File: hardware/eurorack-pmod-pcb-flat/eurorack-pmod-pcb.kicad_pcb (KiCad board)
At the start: 4 copper layers, 40 x 110 mm, 104 parts, among them J1 EURORACK_PWR, J10 PJ398SM, J2 PMOD, J3 PJ398SM, J4 PJ398SM, J5 PJ398SM, J6 PJ398SM, J7 PJ398SM, J8 PJ398SM, J9 PJ398SM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

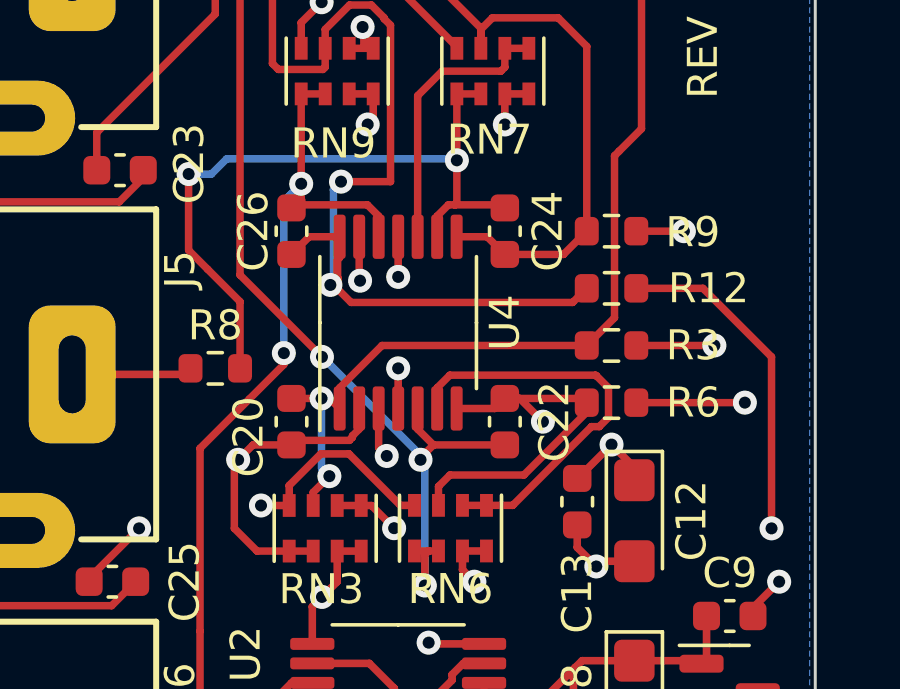
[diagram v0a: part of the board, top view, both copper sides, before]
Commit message: rev3: add notes, fix flipped op-amp
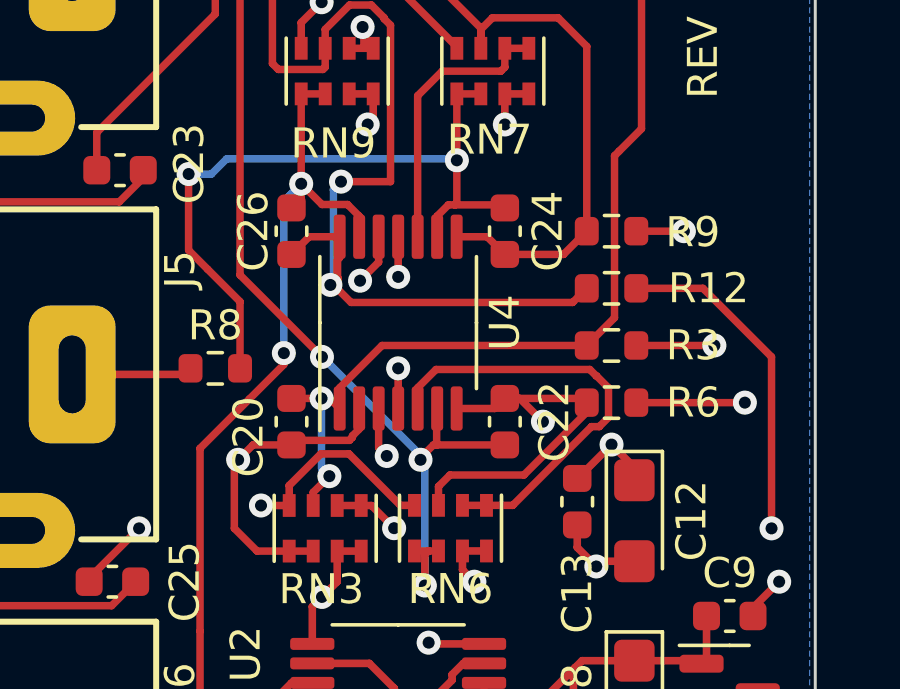
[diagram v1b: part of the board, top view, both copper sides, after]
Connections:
- U4 pad 12: Net-(C26-Pad1) -> Net-(RN9-Pad5)
- U4 pad 13: Net-(RN9-Pad5) -> Net-(C26-Pad1)
- U4 pad 5: Net-(C22-Pad1) -> Net-(RN6-Pad5)
- U4 pad 6: Net-(RN6-Pad5) -> Net-(C22-Pad1)
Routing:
- net Net-(RN6-Pad5): track 13.8 -> 14.6 mm
- net Net-(C26-Pad1): track 30.6 -> 29.9 mm
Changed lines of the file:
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@@
       (net 7 "+12V") (pinfunction "V+") (pintype "power_in"))
     (pad "5" smd roundrect (at -2.8625 0.65 90) (size 1.475 0.4) (layers "F.Cu" "F.Paste" "F.Mask") (roundrect_rratio 0.25)
-      (net 58 "Net-(C22-Pad1)") (pinfunction "+") (pintype "input"))
+      (net 49 "Net-(RN6-Pad5)") (pinfunction "+") (pintype "input"))
     (pad "6" smd roundrect (at -2.8625 1.3 90) (size 1.475 0.4) (layers "F.Cu" "F.Paste" "F.Mask") (roundrect_rratio 0.25)
-      (net 49 "Net-(RN6-Pad5)") (pinfunction "-") (pintype "input"))
+      (net 58 "Net-(C22-Pad1)") (pinfunction "-") (pintype "input"))
     (pad "7" smd roundrect (at -2.8625 1.95 90) (size 1.475 0.4) (layers "F.Cu" "F.Paste" "F.Mask") (roundrect_rratio 0.25)
       (net 59 "Net-(C22-Pad2)") (pintype "output"))
@@
       (net 8 "-12V") (pinfunction "V-") (pintype "power_in"))
     (pad "12" smd roundrect (at 2.8625 -0.65 90) (size 1.475 0.4) (layers "F.Cu" "F.Paste" "F.Mask") (roundrect_rratio 0.25)
-      (net 68 "Net-(C26-Pad1)") (pinfunction "+") (pintype "input"))
+      (net 82 "Net-(RN9-Pad5)") (pinfunction "+") (pintype "input"))
     (pad "13" smd roundrect (at 2.8625 -1.3 90) (size 1.475 0.4) (layers "F.Cu" "F.Paste" "F.Mask") (roundrect_rratio 0.25)
-      (net 82 "Net-(RN9-Pad5)") (pinfunction "-") (pintype "input"))
+      (net 68 "Net-(C26-Pad1)") (pinfunction "-") (pintype "input"))
     (pad "14" smd roundrect (at 2.8625 -1.95 90) (size 1.475 0.4) (layers "F.Cu" "F.Paste" "F.Mask") (roundrect_rratio 0.25)
       (net 70 "Net-(C26-Pad2)") (pintype "output"))
@@
   (segment (start 0.889 18.288) (end 0 19.177) (width 0.25) (layer "In1.Cu") (net 48))
   (segment (start 0 35.306) (end 0.762 36.068) (width 0.25) (layer "In1.Cu") (net 48))
-  (segment (start 9.040295 37.587713) (end 9.91447 37.587713) (width 0.25) (layer "F.Cu") (net 49))
+  (segment (start 12.800462 34.963) (end 12.539183 34.963) (width 0.25) (layer "F.Cu") (net 49))
+  (segment (start 12.539183 34.963) (end 9.91447 37.587713) (width 0.25) (layer "F.Cu") (net 49))
+  (segment (start 13.108 33.670538) (end 13.108 34.655462) (width 0.25) (layer "F.Cu") (net 49))
+  (segment (start 7.357959 33.058) (end 12.484 33.058) (width 0.25) (layer "F.Cu") (net 49))
   (segment (start 8.240295 37.587713) (end 9.040295 37.587713) (width 0.25) (layer "F.Cu") (net 49))
-  (segment (start 12.711462 33.274) (end 12.7 33.274) (width 0.25) (layer "F.Cu") (net 49))
-  (segment (start 7.396 33.669959) (end 7.396 34.3585) (width 0.25) (layer "F.Cu") (net 49))
-  (segment (start 12.7 33.274) (end 12.674 33.248) (width 0.25) (layer "F.Cu") (net 49))
-  (segment (start 12.539183 34.963) (end 12.800462 34.963) (width 0.25) (layer "F.Cu") (net 49))
-  (segment (start 13.108 34.655462) (end 13.108 33.670538) (width 0.25) (layer "F.Cu") (net 49))
-  (segment (start 12.674 33.248) (end 7.817959 33.248) (width 0.25) (layer "F.Cu") (net 49))
-  (segment (start 7.817959 33.248) (end 7.396 33.669959) (width 0.25) (layer "F.Cu") (net 49))
-  (segment (start 9.91447 37.587713) (end 12.539183 34.963) (width 0.25) (layer "F.Cu") (net 49))
-  (segment (start 13.108 33.670538) (end 12.711462 33.274) (width 0.25) (layer "F.Cu") (net 49))
-  (segment (start 12.800462 34.963) (end 13.108 34.655462) (width 0.25) (layer "F.Cu") (net 49))
+  (segment (start 9.91447 37.587713) (end 9.040295 37.587713) (width 0.25) (layer "F.Cu") (net 49))
+  (segment (start 13.108 34.655462) (end 12.800462 34.963) (width 0.25) (layer "F.Cu") (net 49))
+  (segment (start 12.711462 33.274) (end 13.108 33.670538) (width 0.25) (layer "F.Cu") (net 49))
+  (segment (start 6.746 33.669959) (end 7.357959 33.058) (width 0.25) (layer "F.Cu") (net 49))
+  (segment (start 12.7 33.274) (end 12.711462 33.274) (width 0.25) (layer "F.Cu") (net 49))
+  (segment (start 6.746 34.3585) (end 6.746 33.669959) (width 0.25) (layer "F.Cu") (net 49))
+  (segment (start 12.484 33.058) (end 12.7 33.274) (width 0.25) (layer "F.Cu") (net 49))
   (segment (start 6.42 64.645) (end 6.42 64.205) (width 0.25) (layer "F.Cu") (net 50))
   (segment (start 6.42 64.205) (end 5.969 63.754) (width 0.25) (layer "F.Cu") (net 50))
@@
   (segment (start 7.103713 39.107713) (end 7.440295 39.107713) (width 0.25) (layer "F.Cu") (net 58))
   (segment (start 7.271959 35.573) (end 6.841503 36.003456) (width 0.25) (layer "F.Cu") (net 58))
-  (segment (start 9.652 35.573) (end 7.271959 35.573) (width 0.25) (layer "F.Cu") (net 58))
   (segment (start 6.985 40.259) (end 6.985 39.226426) (width 0.25) (layer "F.Cu") (net 58))
   (segment (start 6.841503 36.003456) (end 6.841503 36.068) (width 0.25) (layer "F.Cu") (net 58))
-  (segment (start 6.746 35.047041) (end 6.746 34.3585) (width 0.25) (layer "F.Cu") (net 58))
+  (segment (start 7.379 34.3755) (end 7.379 35.573) (width 0.25) (layer "F.Cu") (net 58))
+  (segment (start 7.396 34.3585) (end 7.379 34.3755) (width 0.25) (layer "F.Cu") (net 58))
+  (segment (start 9.652 35.573) (end 7.379 35.573) (width 0.25) (layer "F.Cu") (net 58))
   (segment (start 0.825 19.685) (end 0.825 29.908) (width 0.25) (layer "F.Cu") (net 58))
-  (segment (start 7.271959 35.573) (end 6.746 35.047041) (width 0.25) (layer "F.Cu") (net 58))
   (segment (start 6.640295 39.107713) (end 7.103713 39.107713) (width 0.25) (layer "F.Cu") (net 58))
+  (segment (start 7.379 35.573) (end 7.271959 35.573) (width 0.25) (layer "F.Cu") (net 58))
   (via (at 3.556 32.639) (size 0.8) (drill 0.4) (layers "F.Cu" "B.Cu") (net 58))
   (via (at 6.841503 36.068) (size 0.8) (drill 0.4) (layers "F.Cu" "B.Cu") (net 58))
@@
   (segment (start -2.667 84.455) (end -1.651 84.455) (width 0.25) (layer "In2.Cu") (net 67))
   (segment (start 0.825 46.99) (end -0.508 45.657) (width 0.25) (layer "F.Cu") (net 68))
-  (segment (start 5.446 27.944959) (end 5.446 28.6335) (width 0.25) (layer "F.Cu") (net 68))
   (segment (start 2.864 27.349) (end 2.864 23.872) (width 0.25) (layer "F.Cu") (net 68))
-  (segment (start 2.54 27.673) (end 2.642 27.571) (width 0.25) (layer "F.Cu") (net 68))
-  (segment (start 2.642 27.571) (end 5.072041 27.571) (width 0.25) (layer "F.Cu") (net 68))
-  (segment (start 5.072041 27.571) (end 5.446 27.944959) (width 0.25) (layer "F.Cu") (net 68))
+  (segment (start 4.410041 27.559) (end 3.556 27.559) (width 0.25) (layer "F.Cu") (net 68))
+  (segment (start 3.556 27.559) (end 2.864 26.867) (width 0.25) (layer "F.Cu") (net 68))
   (segment (start 1.143 34.036) (end 2.286 32.893) (width 0.25) (layer "F.Cu") (net 68))
   (segment (start -0.508 41.783) (end -0.508 35.687) (width 0.25) (layer "F.Cu") (net 68))
@@
   (segment (start 2.286 32.893) (end 2.286 32.512) (width 0.25) (layer "F.Cu") (net 68))
   (segment (start -0.508 45.657) (end -0.508 41.783) (width 0.25) (layer "F.Cu") (net 68))
+  (segment (start 4.796 28.6335) (end 4.796 27.944959) (width 0.25) (layer "F.Cu") (net 68))
   (segment (start -0.508 35.687) (end 1.143 34.036) (width 0.25) (layer "F.Cu") (net 68))
   (segment (start 3.664 23.872) (end 2.864 23.872) (width 0.25) (layer "F.Cu") (net 68))
+  (segment (start 4.796 27.944959) (end 4.410041 27.559) (width 0.25) (layer "F.Cu") (net 68))
   (via (at 2.864 26.867) (size 0.8) (drill 0.4) (layers "F.Cu" "B.Cu") (net 68))
   (via (at 2.286 32.512) (size 0.8) (drill 0.4) (layers "F.Cu" "B.Cu") (net 68))
@@
   (segment (start 2.414094 70.867094) (end 0.095999 70.867094) (width 0.25) (layer "B.Cu") (net 81))
   (segment (start 2.794 71.247) (end 2.414094 70.867094) (width 0.25) (layer "B.Cu") (net 81))
-  (segment (start 4.796 28.6335) (end 4.796 30.069) (width 0.25) (layer "F.Cu") (net 82))
+  (segment (start 5.446 29.479) (end 5.446 28.6335) (width 0.25) (layer "F.Cu") (net 82))
   (segment (start 4.953 22.352) (end 5.264 22.352) (width 0.25) (layer "F.Cu") (net 82))
   (segment (start 4.953 22.352) (end 4.953 21.683246) (width 0.25) (layer "F.Cu") (net 82))
   (segment (start 4.953 21.683246) (end 4.910676 21.640922) (width 0.25) (layer "F.Cu") (net 82))
   (segment (start 4.464 22.352) (end 4.953 22.352) (width 0.25) (layer "F.Cu") (net 82))
-  (segment (start 4.796 30.069) (end 4.826 30.099) (width 0.25) (layer "F.Cu") (net 82))
+  (segment (start 4.826 30.099) (end 5.446 29.479) (width 0.25) (layer "F.Cu") (net 82))
   (via (at 4.826 30.099) (size 0.8) (drill 0.4) (layers "F.Cu" "B.Cu") (net 82))
   (via (at 4.910676 21.640922) (size 0.8) (drill 0.4) (layers "F.Cu" "B.Cu") (net 82))

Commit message: rev2.2: move LEDs over and generate fab2
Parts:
- moved D10 0.18 mm to (-17.4, 108.7)
- moved D3 0.18 mm to (-17.4, 12.6)
- moved D7 0.18 mm to (-17.4, 67.6)
- moved D4 0.18 mm to (-17.4, 26.3)
- moved D5 0.18 mm to (-17.4, 40.1)
- moved D6 0.18 mm to (-17.4, 53.8)
- moved D8 0.18 mm to (-17.4, 81.3)
- moved D9 0.18 mm to (-17.4, 95.1)
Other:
- board text added: "REV 2.2 2022-09-10"
- board text removed: "REV 2.1 2022-07-30"
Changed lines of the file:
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@@
       (drillshape 0)
       (scaleselection 1)
-      (outputdirectory "fab1/")
+      (outputdirectory "fab2/")
     )
   )
@@
   )
   (footprint "LED_SMD:LED_1206_3216Metric" (layer "F.Cu")
-    (at -17.2466 81.3308)
+    (at -17.4244 81.3308)
     (descr "LED SMD 1206 (3216 Metric), square (rectangular) end terminal, IPC_7351 nominal, (Body size source: http://www.tortai-tech.com/upload/download/2011102023233369053.pdf), generated with kicad-footprint-generator")
     (tags "LED")
@@
   )
   (footprint "LED_SMD:LED_1206_3216Metric" (layer "F.Cu")
-    (at -17.2466 40.0812)
+    (at -17.4244 40.0812)
     (descr "LED SMD 1206 (3216 Metric), square (rectangular) end terminal, IPC_7351 nominal, (Body size source: http://www.tortai-tech.com/upload/download/2011102023233369053.pdf), generated with kicad-footprint-generator")
     (tags "LED")
@@
   )
   (footprint "LED_SMD:LED_1206_3216Metric" (layer "F.Cu")
-    (at -17.2212 67.564)
+    (at -17.399 67.564)
     (descr "LED SMD 1206 (3216 Metric), square (rectangular) end terminal, IPC_7351 nominal, (Body size source: http://www.tortai-tech.com/upload/download/2011102023233369053.pdf), generated with kicad-footprint-generator")
     (tags "LED")
@@
   )
   (footprint "LED_SMD:LED_1206_3216Metric" (layer "F.Cu")
-    (at -17.2466 53.8226)
+    (at -17.4244 53.8226)
     (descr "LED SMD 1206 (3216 Metric), square (rectangular) end terminal, IPC_7351 nominal, (Body size source: http://www.tortai-tech.com/upload/download/2011102023233369053.pdf), generated with kicad-footprint-generator")
     (tags "LED")
@@
   )
   (footprint "LED_SMD:LED_1206_3216Metric" (layer "F.Cu")
-    (at -17.2212 12.5984)
+    (at -17.399 12.5984)
     (descr "LED SMD 1206 (3216 Metric), square (rectangular) end terminal, IPC_7351 nominal, (Body size source: http://www.tortai-tech.com/upload/download/2011102023233369053.pdf), generated with kicad-footprint-generator")
     (tags "LED")
@@
   )
   (footprint "LED_SMD:LED_1206_3216Metric" (layer "F.Cu")
-    (at -17.2436 26.3398)
+    (at -17.4214 26.3398)
     (descr "LED SMD 1206 (3216 Metric), square (rectangular) end terminal, IPC_7351 nominal, (Body size source: http://www.tortai-tech.com/upload/download/2011102023233369053.pdf), generated with kicad-footprint-generator")
     (tags "LED")
@@
     (fp_line (start 1.6 -0.8) (end -1.2 -0.8) (layer "F.Fab") (width 0.1))
     (fp_line (start -1.6 0.8) (end 1.6 0.8) (layer "F.Fab") (width 0.1))
-    (pad "1" smd roundrect (at -1.35 0 270) (size 1.4 1.35) (layers "F.Cu" "F.Paste" "F.Mask") (roundrect_rratio 0.185185)
+    (pad "1" smd roundrect (at -1.35 0 270) (size 1.4 1.35) (layers "F.Cu" "F.Paste" "F.Mask") (roundrect_rratio 0.1851851852)
       (net 91 "/VREFH") (pintype "passive"))
-    (pad "2" smd roundrect (at 1.35 0 270) (size 1.4 1.35) (layers "F.Cu" "F.Paste" "F.Mask") (roundrect_rratio 0.185185)
+    (pad "2" smd roundrect (at 1.35 0 270) (size 1.4 1.35) (layers "F.Cu" "F.Paste" "F.Mask") (roundrect_rratio 0.1851851852)
       (net 2 "GND") (pintype "passive"))
     (model "${KICAD6_3DMODEL_DIR}/Capacitor_Tantalum_SMD.3dshapes/CP_EIA-3216-10_Kemet-I.wrl"
@@
   )
   (footprint "LED_SMD:LED_1206_3216Metric" (layer "F.Cu")
-    (at -17.2212 108.6866)
+    (at -17.399 108.6866)
     (descr "LED SMD 1206 (3216 Metric), square (rectangular) end terminal, IPC_7351 nominal, (Body size source: http://www.tortai-tech.com/upload/download/2011102023233369053.pdf), generated with kicad-footprint-generator")
     (tags "LED")
@@
   )
   (footprint "LED_SMD:LED_1206_3216Metric" (layer "F.Cu")
-    (at -17.2466 95.0722)
+    (at -17.4244 95.0722)
     (descr "LED SMD 1206 (3216 Metric), square (rectangular) end terminal, IPC_7351 nominal, (Body size source: http://www.tortai-tech.com/upload/download/2011102023233369053.pdf), generated with kicad-footprint-generator")
     (tags "LED")
@@
     (effects (font (size 1 1) (thickness 0.25)))
   )
-  (gr_text "REV 2.1 2022-07-30" (at 16.256 17.145 -270) (layer "F.SilkS")
+  (gr_text "REV 2.2 2022-09-10" (at 16.256 17.145 -270) (layer "F.SilkS")
     (effects (font (size 1 1) (thickness 0.25)))
   )
@@
   (segment (start -13.7028 108.6866) (end -13.6774 108.712) (width 0.25) (layer "F.Cu") (net 52))
   (segment (start -15.8212 108.6866) (end -13.7028 108.6866) (width 0.25) (layer "F.Cu") (net 52))
-  (via (at -17.145 108.712) (size 0.8) (drill 0.4) (layers "F.Cu" "B.Cu") (net 52))
+  (via (at -17.399 108.6866) (size 0.8) (drill 0.4) (layers "F.Cu" "B.Cu") (net 52))
   (via (at 3.683 88.138) (size 0.8) (drill 0.4) (layers "F.Cu" "B.Cu") (net 52))
-  (segment (start 4.953 89.916) (end 4.953 89.408) (width 0.25) (layer "In2.Cu") (net 52))
-  (segment (start -6.604 98.171) (end -2.286 98.171) (width 0.25) (layer "In2.Cu") (net 52))
-  (segment (start -2.286 98.171) (end -1.397 98.171) (width 0.25) (layer "In2.Cu") (net 52))
-  (segment (start 4.953 91.821) (end 4.953 89.916) (width 0.25) (layer "In2.Cu") (net 52))
-  (segment (start -1.397 98.171) (end 4.445 92.329) (width 0.25) (layer "In2.Cu") (net 52))
-  (segment (start -17.145 108.712) (end -6.604 98.171) (width 0.25) (layer "In2.Cu") (net 52))
+  (segment (start -6.604 98.171) (end -1.397 98.171) (width 0.25) (layer "In2.Cu") (net 52))
+  (segment (start -17.399 108.6866) (end -17.1196 108.6866) (width 0.25) (layer "In2.Cu") (net 52))
+  (segment (start -17.1196 108.6866) (end -6.604 98.171) (width 0.25) (layer "In2.Cu") (net 52))
+  (segment (start -1.397 98.171) (end 4.953 91.821) (width 0.25) (layer "In2.Cu") (net 52))
   (segment (start 4.953 89.408) (end 3.683 88.138) (width 0.25) (layer "In2.Cu") (net 52))
-  (segment (start 4.445 92.329) (end 4.953 91.821) (width 0.25) (layer "In2.Cu") (net 52))
+  (segment (start 4.953 91.821) (end 4.953 89.408) (width 0.25) (layer "In2.Cu") (net 52))
   (segment (start 7.493 9.271) (end 7.904 8.86) (width 0.25) (layer "F.Cu") (net 53))
   (segment (start 2.921 9.271) (end 7.493 9.271) (width 0.25) (layer "F.Cu") (net 53))
